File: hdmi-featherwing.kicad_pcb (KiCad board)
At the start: 2 copper layers, 22.9 x 50.8 mm, 13 parts, among them J1 HDMI_A

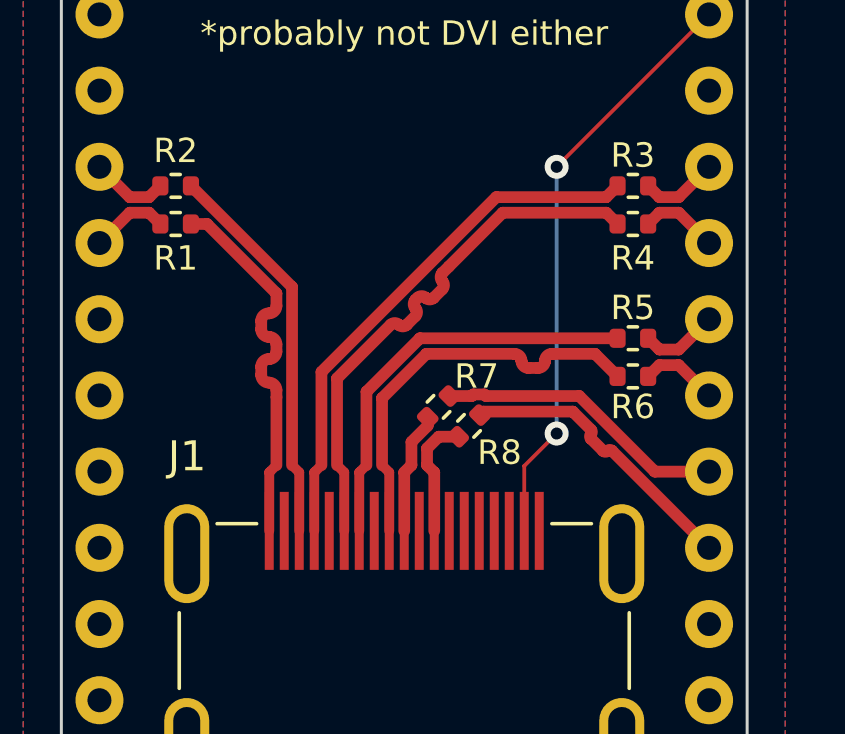
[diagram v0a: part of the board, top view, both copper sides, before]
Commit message: account for Feather in length matching
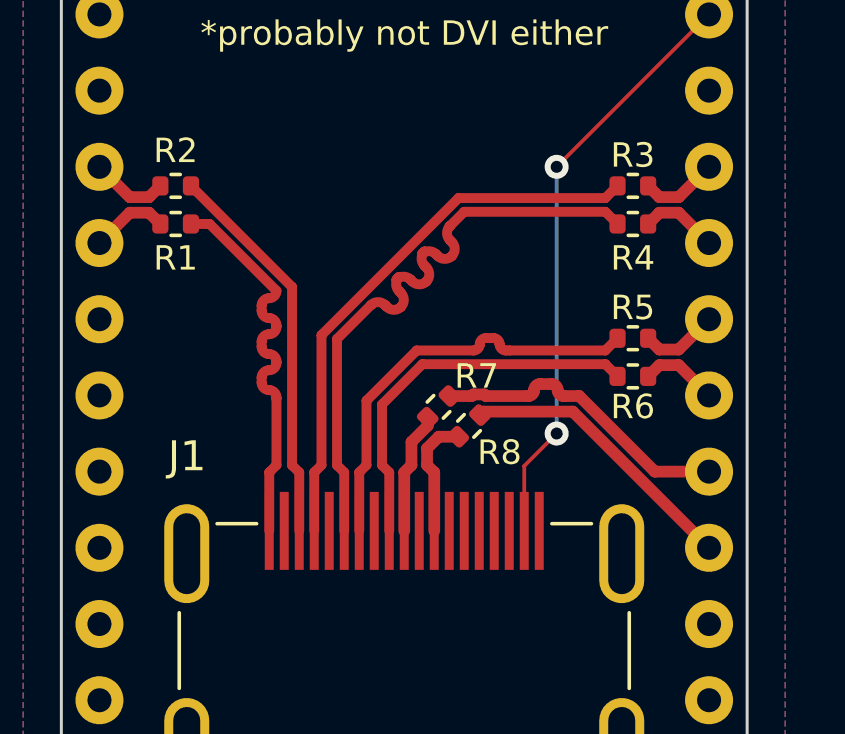
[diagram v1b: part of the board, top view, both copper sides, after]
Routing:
- net /D1-: track 17.8 -> 20.9 mm
- net /D0-: track 13.8 -> 12.9 mm
- net /D1+: track 17.8 -> 18.6 mm
- net /D2+: track 12.9 -> 13.5 mm

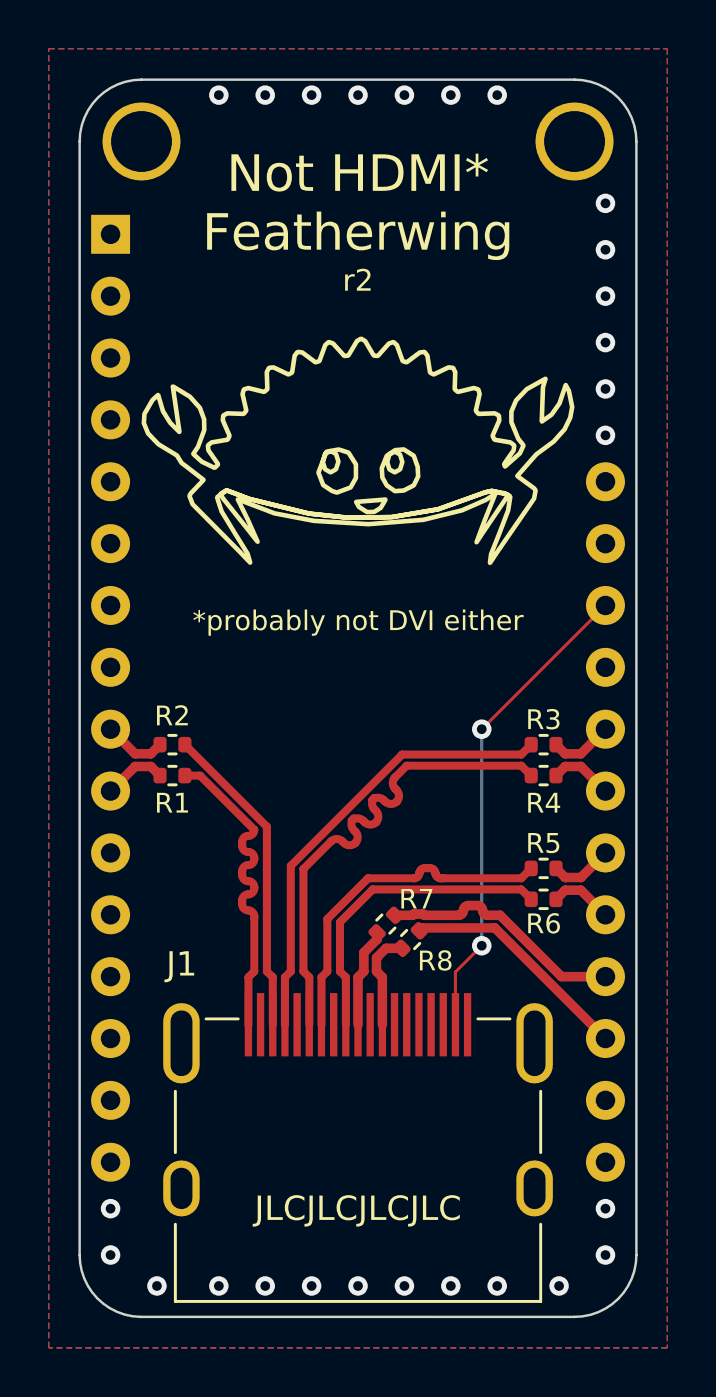
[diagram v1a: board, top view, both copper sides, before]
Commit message: better route resistors
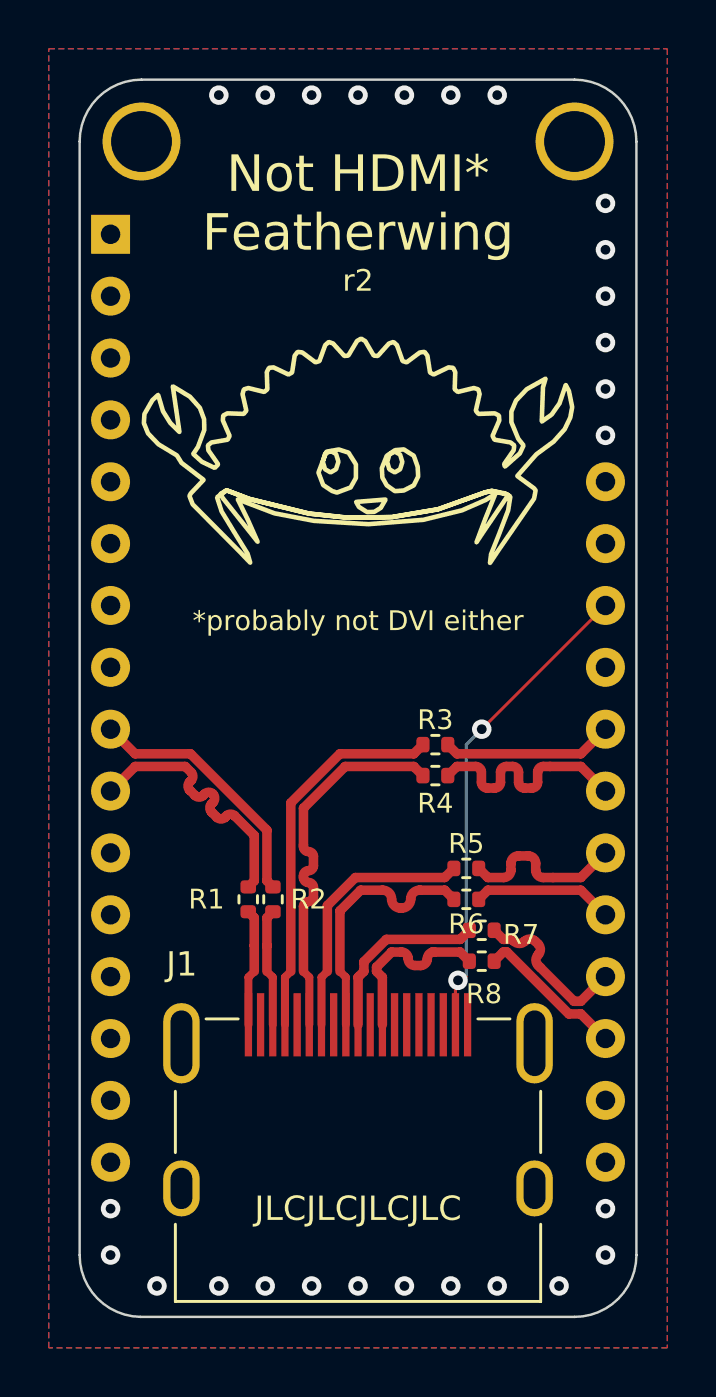
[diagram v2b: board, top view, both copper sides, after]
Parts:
- moved R2 7.57 mm to (115.9, 112.4), turned to -90 degrees
- moved R1 5.96 mm to (114.9, 112.4), turned to -90 degrees
- moved R3 4.44 mm to (122.6, 106.0)
- moved R4 4.44 mm to (122.6, 107.3)
- moved R7 3.95 mm to (124.5, 113.7), turned to 180 degrees
- moved R5 3.17 mm to (123.8, 111.1)
- moved R6 3.17 mm to (123.8, 112.4)
- moved R8 3.05 mm to (124.5, 114.9), turned to 180 degrees
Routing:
- net /D2+: track 13.5 -> 4.84 mm
- net /WING_D2+: track 2.60 -> 11.1 mm
- net /D2-: track 13.0 -> 4.84 mm
- net /WING_D2-: track 2.60 -> 10.6 mm
- net /WING_D1-: track 2.60 -> 9.71 mm
- net /D1-: track 20.9 -> 15.6 mm
- net /WING_D1+: track 2.60 -> 7.05 mm
- net /WING_D0+: track 2.60 -> 6.98 mm
- net /CK+: track 4.10 -> 7.55 mm
- net /WING_CK-: track 9.57 -> 6.20 mm
- net /CK-: track 4.05 -> 7.41 mm
- net /WING_CK+: track 10.2 -> 6.85 mm
- net /D0+: track 14.1 -> 10.8 mm
- net /WING_D0-: track 2.60 -> 5.78 mm
- net /D1+: track 18.6 -> 15.6 mm
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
